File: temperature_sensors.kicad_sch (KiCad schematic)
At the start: 32 parts, among them J3 Conn_01x04_Pin, J4 Conn_01x04_Pin, J5 Conn_01x04_Pin, J6 Conn_01x04_Pin

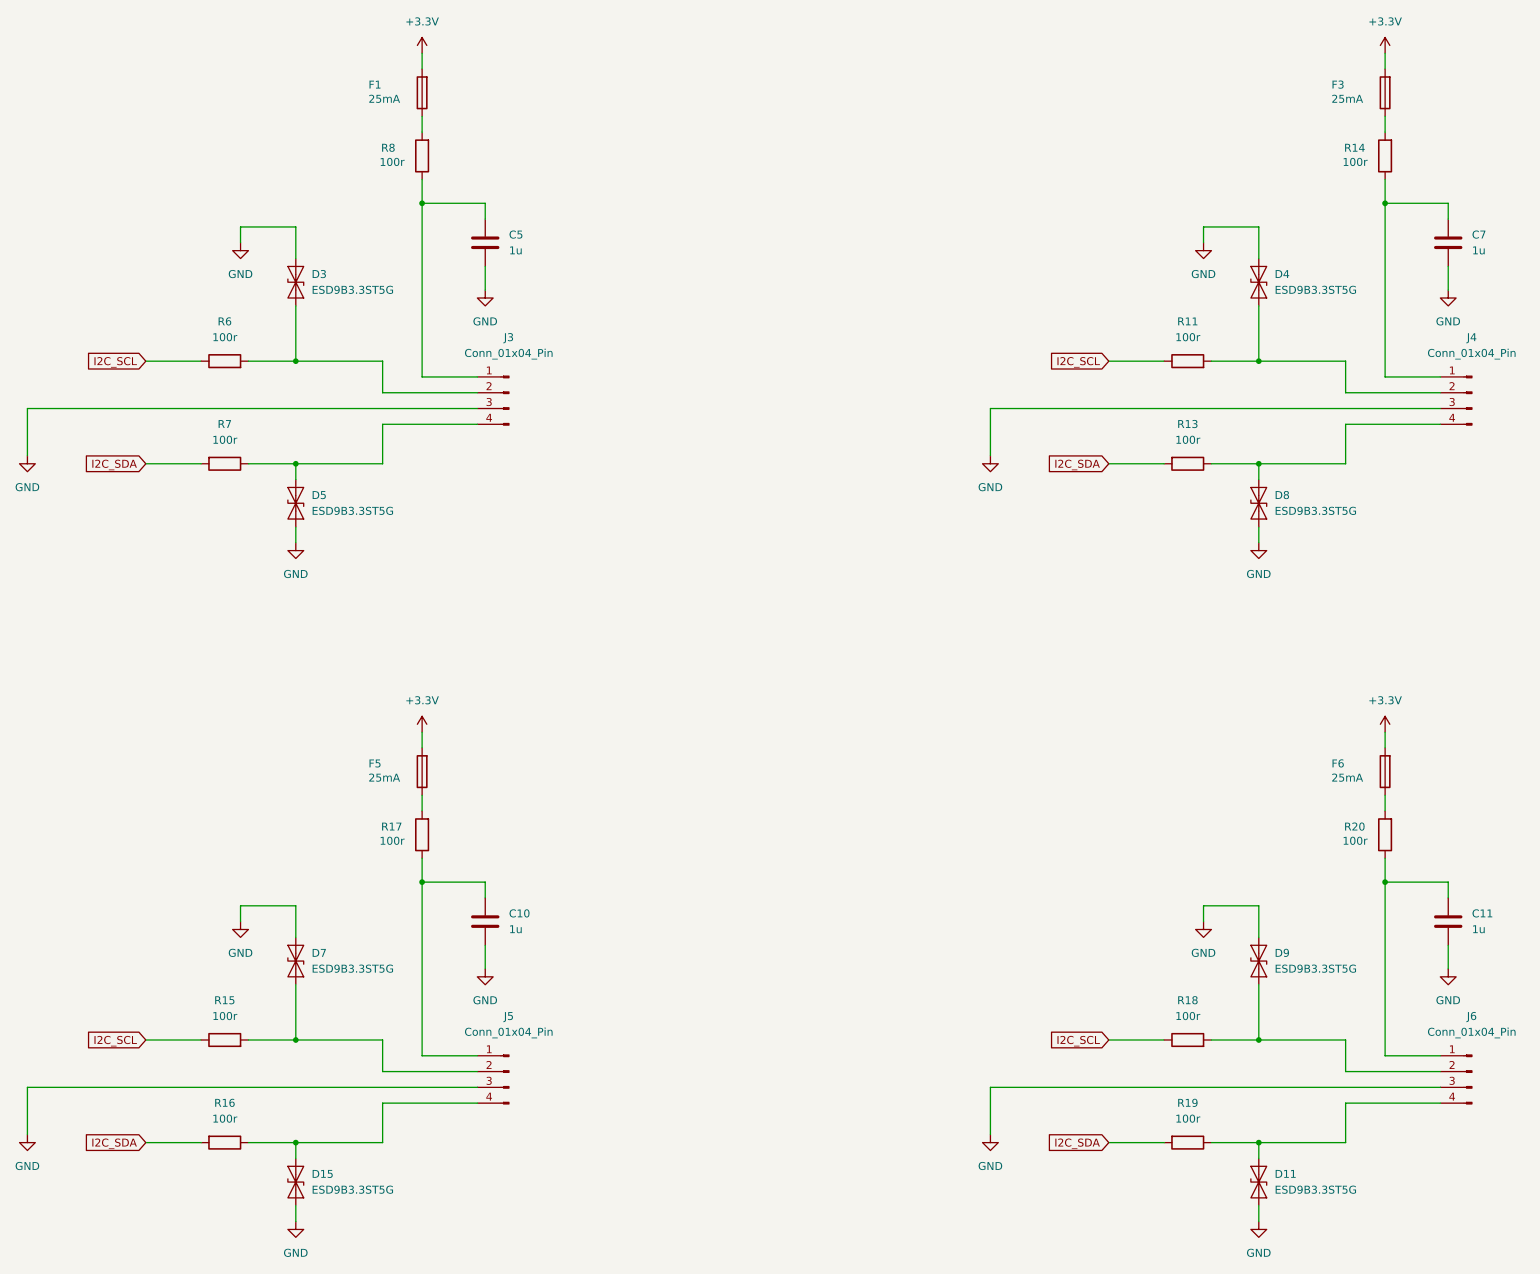
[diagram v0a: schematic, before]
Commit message: changed I2C temp sensor to thermistor
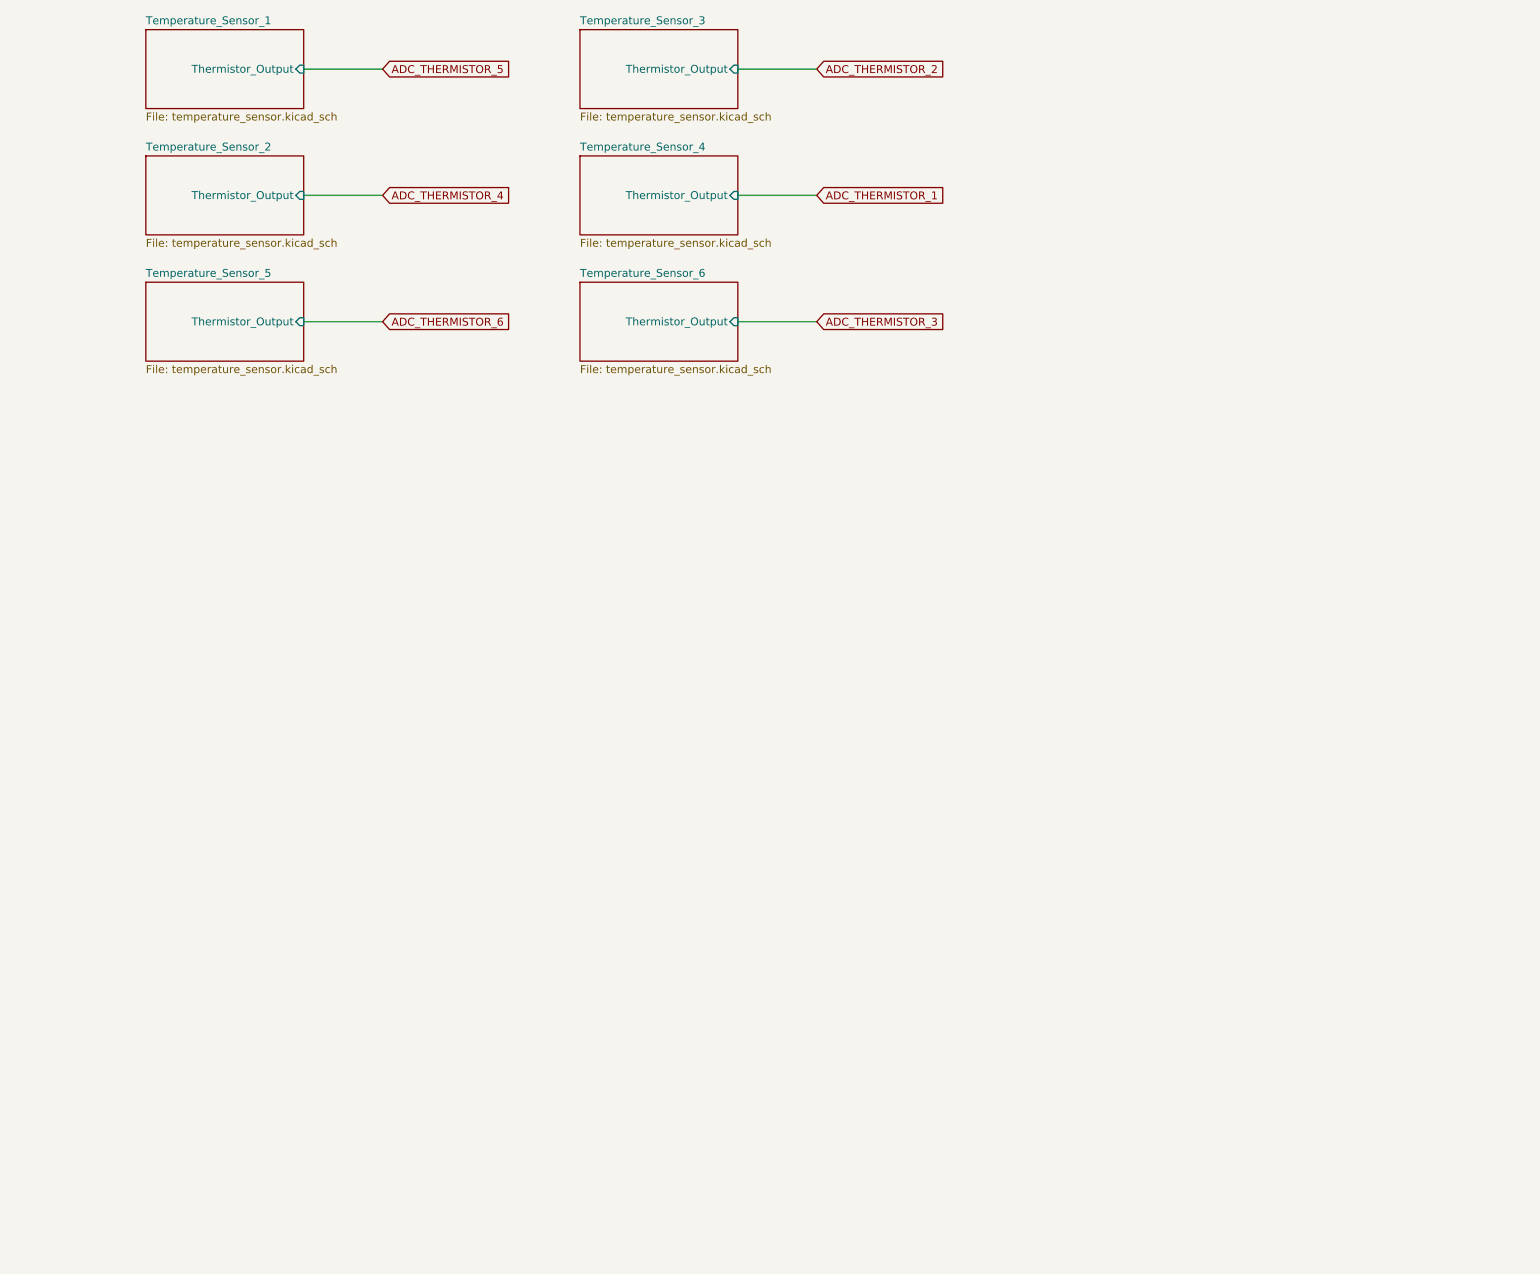
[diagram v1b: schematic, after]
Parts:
- removed C10, C11, C5, C7: 1u, Capacitor_SMD:C_0603_1608Metric_Pad1.08x0.95mm_HandSolder, symbol Device:C
- removed D11, D15, D3, D4, D5, D7, D8, D9: ESD9B3.3ST5G, Diode_SMD:D_SOD-923, symbol Diode:ESD9B3.3ST5G
- removed F1, F3, F5, F6: 25mA, Fuse:Fuse_1206_3216Metric_Pad1.42x1.75mm_HandSolder, symbol Device:Fuse
- removed J3, J4, J5, J6: Conn_01x04_Pin, Connector_JST:JST_GH_BM04B-GHS-TBT_1x04-1MP_P1.25mm_Vertical, symbol Connector:Conn_01x04_Pin
- removed R11, R13, R14, R15, R16, R17, R18, R19, R20, R6, R7, R8: 100r, Resistor_SMD:R_0603_1608Metric_Pad0.98x0.95mm_HandSolder, symbol Device:R
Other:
- added sheet Temperature_Sensor_1 (temperature_sensor.kicad_sch)
- added sheet Temperature_Sensor_2 (temperature_sensor.kicad_sch)
- added sheet Temperature_Sensor_3 (temperature_sensor.kicad_sch)
- added sheet Temperature_Sensor_4 (temperature_sensor.kicad_sch)
- added sheet Temperature_Sensor_5 (temperature_sensor.kicad_sch)
- added sheet Temperature_Sensor_6 (temperature_sensor.kicad_sch)
